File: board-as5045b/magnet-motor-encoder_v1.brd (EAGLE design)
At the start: 21.9 x 22 mm, 14 parts, among them IC1 AS5045B, IC3 DS18B20

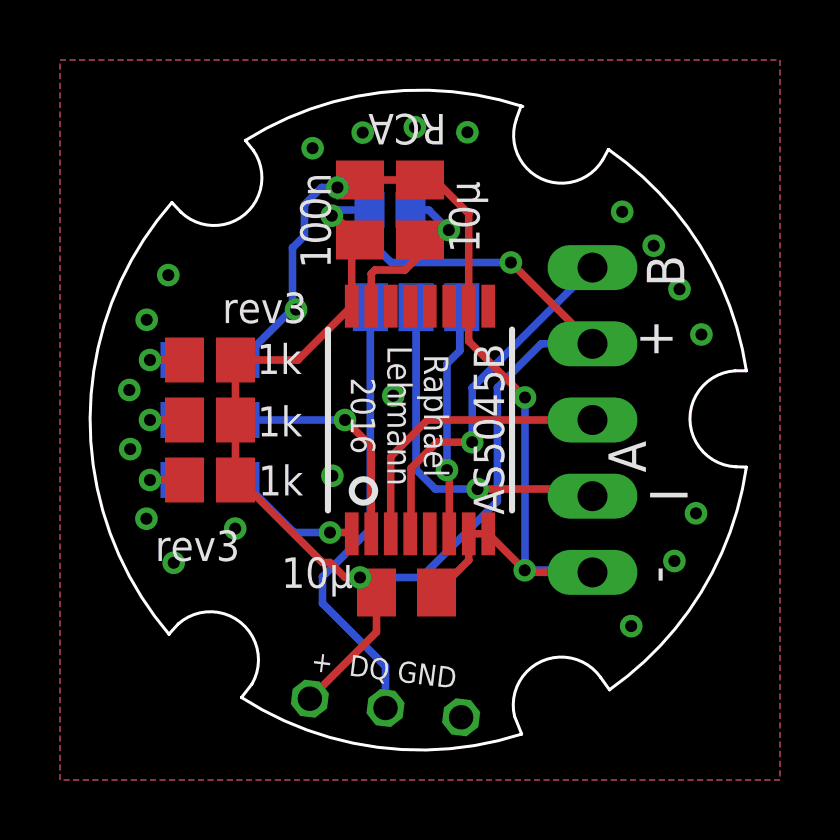
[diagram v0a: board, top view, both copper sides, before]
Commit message: board as5045b: new board shape (imported from 3d-model/solidworks); rev4 tag
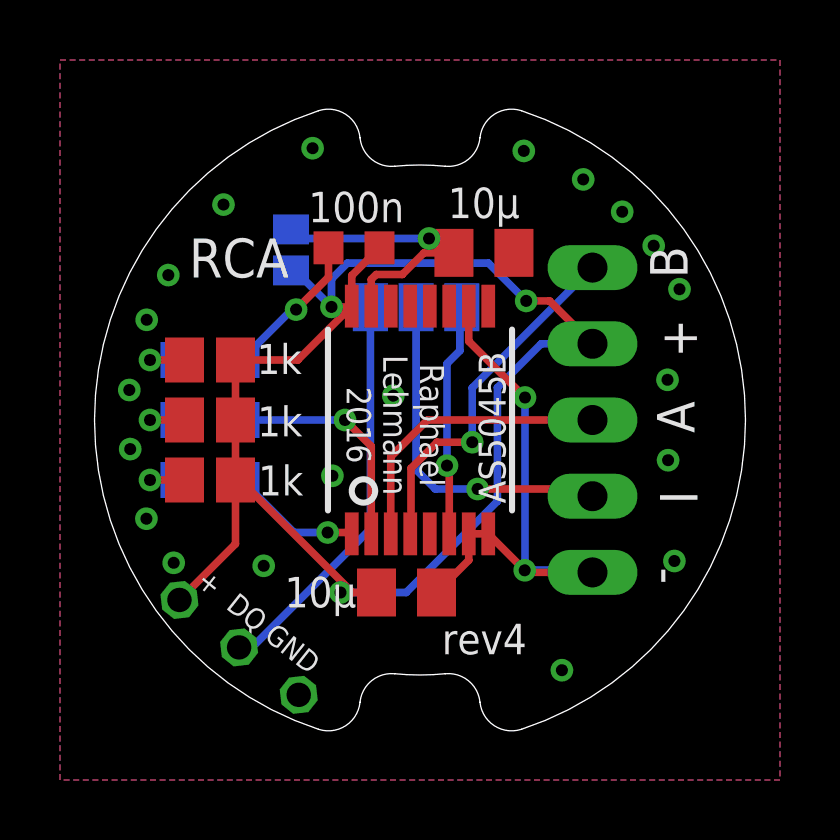
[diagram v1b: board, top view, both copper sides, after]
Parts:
- C1: device resistor:C0805K -> rcl:R0603
- moved IC3 5.28 mm to (-6.03, -7.58), turned to 38.5 degrees
- moved SJ1 3.56 mm to (-4.30, 5.67), turned to 90 degrees
- moved C2 2.57 mm to (2.13, 5.57), turned to 180 degrees
- moved C1 1.28 mm to (-2.20, 5.74), turned to 0 degrees
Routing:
- net GND: track 34.6 -> 24.3 mm, vias 24 -> 23
- net +3V3: track 6.51 -> 9.77 mm
- net +5V: track 48.0 -> 49.9 mm
- net N$3: track 14.9 -> 13.4 mm
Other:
- board size 21.9 x 22 mm -> 21.7 x 20.7 mm
- board text added: "rev4"
- board text removed: "rev3"

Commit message: board as5045b: moved backside resistors; new rev4 tag
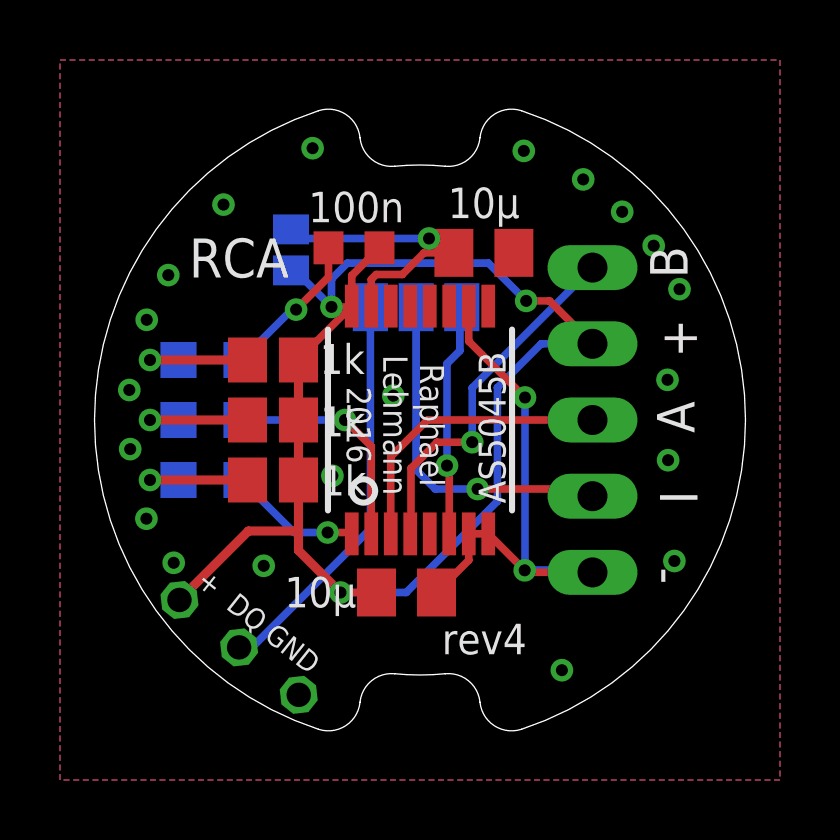
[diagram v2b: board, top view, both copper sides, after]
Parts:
- moved R1 2.10 mm to (-4.90, -2.00)
- moved R2 2.10 mm to (-4.90, 0.00)
- moved R3 2.10 mm to (-4.90, 2.00)
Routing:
- net +5V: track 49.9 -> 46.9 mm
- net R_LED_YELLOW: track 2.10 -> 4.20 mm
- net R_LED_RED: track 2.10 -> 4.20 mm
- net R_LED_BLUE: track 2.30 -> 4.40 mm
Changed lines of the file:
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@@
 <setting verticaltext="up"/>
 </settings>
-<grid distance="0.01" unitdist="mm" unit="mm" style="dots" multiple="1" display="yes" altdistance="0.02" altunitdist="mm" altunit="mm"/>
+<grid distance="0.1" unitdist="mm" unit="mm" style="dots" multiple="1" display="yes" altdistance="0.02" altunitdist="mm" altunit="mm"/>
 <layers>
 <layer number="1" name="Top" color="4" fill="1" visible="yes" active="yes"/>
@@
 <element name="LED_RED" library="led" package="CHIPLED_0805" value="DEC" x="-7" y="0" smashed="yes" rot="MR90"/>
 <element name="LED_BLUE" library="led" package="CHIPLED_0805" value="POWER" x="-7" y="2" smashed="yes" rot="MR90"/>
-<element name="R1" library="resistor" package="R0805" value="1k" x="-7" y="-2" smashed="yes">
-<attribute name="VALUE" x="-5.392" y="-2.516" size="1" layer="25" font="vector"/>
-</element>
-<element name="R2" library="resistor" package="R0805" value="1k" x="-7" y="0" smashed="yes">
-<attribute name="VALUE" x="-5.422" y="-0.546" size="1" layer="25" font="vector"/>
-</element>
-<element name="R3" library="resistor" package="R0805" value="1k" x="-7" y="2" smashed="yes">
-<attribute name="VALUE" x="-5.442" y="1.534" size="1" layer="25" font="vector"/>
+<element name="R1" library="resistor" package="R0805" value="1k" x="-4.9" y="-2" smashed="yes">
+<attribute name="VALUE" x="-3.292" y="-2.516" size="1" layer="25" font="vector"/>
+</element>
+<element name="R2" library="resistor" package="R0805" value="1k" x="-4.9" y="0" smashed="yes">
+<attribute name="VALUE" x="-3.322" y="-0.546" size="1" layer="25" font="vector"/>
+</element>
+<element name="R3" library="resistor" package="R0805" value="1k" x="-4.9" y="2" smashed="yes">
+<attribute name="VALUE" x="-3.342" y="1.534" size="1" layer="25" font="vector"/>
 </element>
 <element name="C1" library="rcl" package="R0603" value="100n" x="-2.2" y="5.74" smashed="yes">
@@
 <wire x1="-8.05" y1="-2" x2="-9" y2="-2" width="0.254" layer="16"/>
 <via x="-9" y="-2" extent="1-16" drill="0.4"/>
-<wire x1="-9" y1="-2" x2="-7.85" y2="-2" width="0.254" layer="1"/>
+<wire x1="-9" y1="-2" x2="-5.75" y2="-2" width="0.3048" layer="1"/>
 </signal>
 <signal name="R_LED_RED">
@@
 <wire x1="-8.05" y1="0" x2="-9" y2="0" width="0.254" layer="16"/>
 <via x="-9" y="0" extent="1-16" drill="0.4"/>
-<wire x1="-9" y1="0" x2="-7.85" y2="0" width="0.254" layer="1"/>
+<wire x1="-9" y1="0" x2="-5.75" y2="0" width="0.3048" layer="1"/>
 </signal>
 <signal name="R_LED_BLUE">
@@
 <wire x1="-7.85" y1="2" x2="-8.05" y2="2" width="0.254" layer="16"/>
 <via x="-9" y="2" extent="1-16" drill="0.4"/>
-<wire x1="-9" y1="2" x2="-7.85" y2="2" width="0.254" layer="1"/>
+<wire x1="-9" y1="2" x2="-5.75" y2="2" width="0.3048" layer="1"/>
 </signal>
 <signal name="+5V">
@@
 <contactref element="C3" pad="2"/>
 <contactref element="JP1" pad="2"/>
-<wire x1="-6.15" y1="2" x2="-4.07" y2="2" width="0.254" layer="1"/>
 <wire x1="-4.07" y1="2" x2="-2.275" y2="3.795" width="0.254" layer="1"/>
 <contactref element="R2" pad="2"/>
 <contactref element="R1" pad="2"/>
-<wire x1="-6.15" y1="2" x2="-6.15" y2="0" width="0.254" layer="1"/>
-<wire x1="-6.15" y1="-2" x2="-6.15" y2="0" width="0.254" layer="1"/>
 <contactref element="IC3" pad="3"/>
-<wire x1="-2.25" y1="-5.75" x2="-6" y2="-2" width="0.254" layer="1"/>
-<wire x1="-6" y1="-2" x2="-6.15" y2="-2" width="0.254" layer="1"/>
 <wire x1="4.04" y1="2.54" x2="2.58" y2="1.08" width="0.254" layer="16"/>
 <wire x1="2.58" y1="1.08" x2="2.58" y2="-2.71" width="0.254" layer="16"/>
@@
 <via x="3.54" y="3.97" extent="1-16" drill="0.4"/>
 <wire x1="3.54" y1="3.97" x2="4.32" y2="3.97" width="0.254" layer="1"/>
-<wire x1="-8.017825" y1="-5.9988125" x2="-6.15" y2="-4.1309875" width="0.254" layer="1"/>
-<wire x1="-6.15" y1="-4.1309875" x2="-6.15" y2="-2" width="0.254" layer="1"/>
 <wire x1="-1.35" y1="5.74" x2="-2.275" y2="4.815" width="0.254" layer="1"/>
 <wire x1="-2.275" y1="4.815" x2="-2.275" y2="3.795" width="0.254" layer="1"/>
@@
 <wire x1="-2.42" y1="5.23" x2="2.28" y2="5.23" width="0.254" layer="16"/>
 <wire x1="3.54" y1="3.97" x2="2.28" y2="5.23" width="0.254" layer="16"/>
-<wire x1="-1.45" y1="-5.75" x2="-2.23" y2="-5.75" width="0.254" layer="1"/>
-<wire x1="-2.23" y1="-5.75" x2="-2.25" y2="-5.75" width="0.254" layer="1"/>
+<wire x1="-1.45" y1="-5.75" x2="-2.65" y2="-5.75" width="0.254" layer="1"/>
 <wire x1="-0.46" y1="-5.75" x2="-2.65" y2="-5.75" width="0.254" layer="16"/>
 <via x="-2.65" y="-5.75" extent="1-16" drill="0.4"/>
-<wire x1="-2.65" y1="-5.75" x2="-2.25" y2="-5.75" width="0.254" layer="1"/>
+<wire x1="-2.65" y1="-5.75" x2="-4.05" y2="-4.35" width="0.3048" layer="1"/>
+<wire x1="-4.05" y1="-4.35" x2="-4.05" y2="-3.7" width="0.3048" layer="1"/>
+<wire x1="-4.05" y1="-3.7" x2="-4.05" y2="-2" width="0.3048" layer="1"/>
+<wire x1="-4.05" y1="-2" x2="-4.05" y2="0" width="0.3048" layer="1"/>
+<wire x1="-4.05" y1="2" x2="-4.05" y2="0" width="0.3048" layer="1"/>
+<wire x1="-8.017825" y1="-5.9988125" x2="-5.7190125" y2="-3.7" width="0.3048" layer="1"/>
+<wire x1="-5.7190125" y1="-3.7" x2="-4.05" y2="-3.7" width="0.3048" layer="1"/>
 </signal>
 <signal name="+3V3">

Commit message: board as5045b: add missing CSn pulldown resistor; new rev5 tag
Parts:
- added R4: 4k7, resistor:R0805
- added U$1: (no value), rca_templates:LOGO_SILK
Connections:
- new net N$4: IC1.11, R4.2
- net GND: now also R4.1
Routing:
- net N$4: track 0.00 -> 5.25 mm, vias 0 -> 1
- net GND: track 24.3 -> 26.0 mm
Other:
- board text added: "INC DEC"
- board text added: "POW"
- board text added: "rev5"
- board text removed: "INC DEC POW"
- board text removed: "rev4"
